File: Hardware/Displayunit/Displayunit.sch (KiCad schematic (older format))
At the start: 111 parts, among them IC1 TSC2007, IC2 MX25LM51245GXDI00, IC3 IS66WVH8M8BLL-100B1LI_0, J1 USB_B_Micro, J2 8P8C_Shielded, J3 54104-4031, J4 Conn_ARM_JTAG_SWD_20, J5 52271-0679, J6 Conn_02x06_Odd_Even, J7 734-264, Q1 2N7002, SW1 Boot, SW2 Reset, SW3 Wakeup, U1 STM32L4R9ZITx, U2 USBLC6-2SC6, U3 STLD40D, U4 MAX17572, U5 MAX17572, U6 SN65HVD231, Y1 16 MHz, Y2 32.768

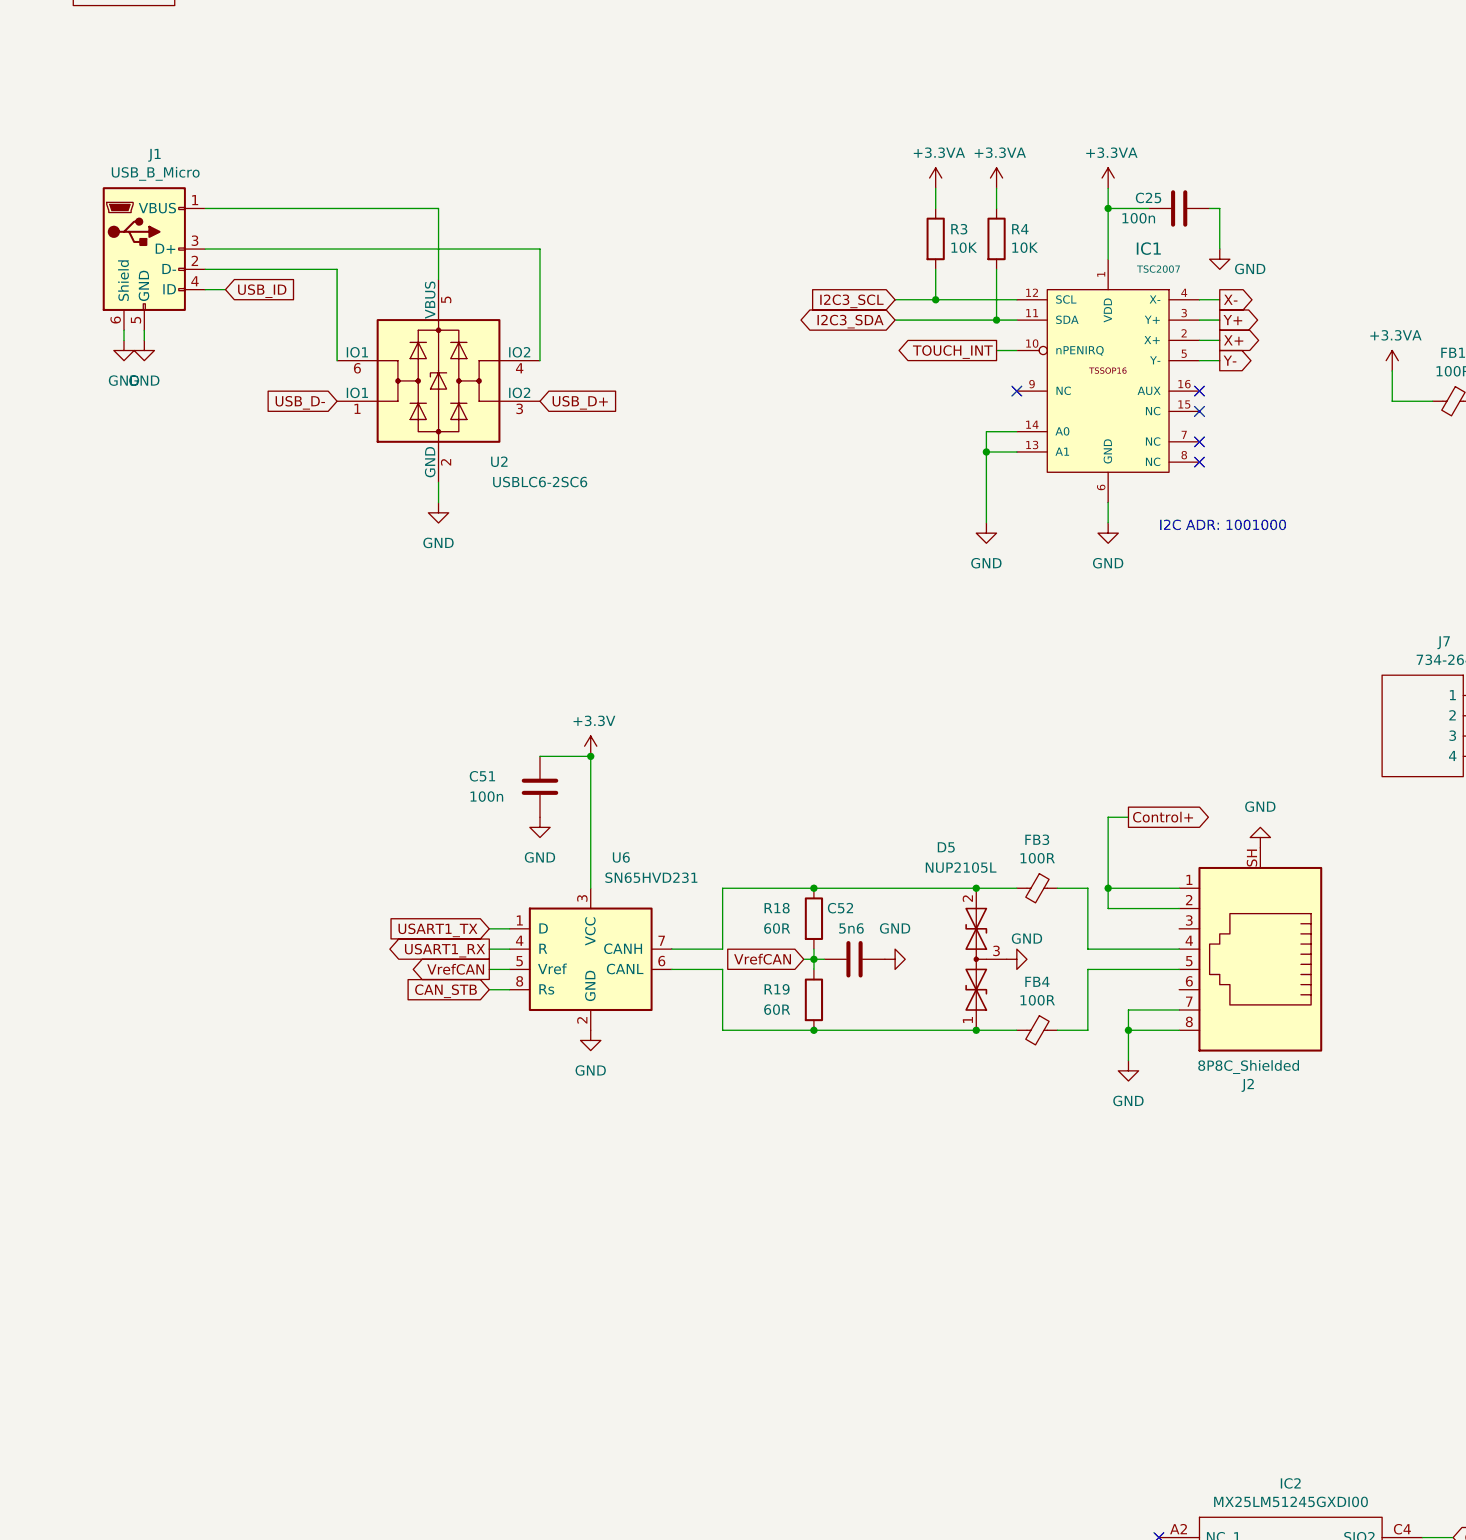
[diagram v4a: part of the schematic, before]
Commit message: Displayunit: Zweite Controlbus Buchse hinzugefügt.
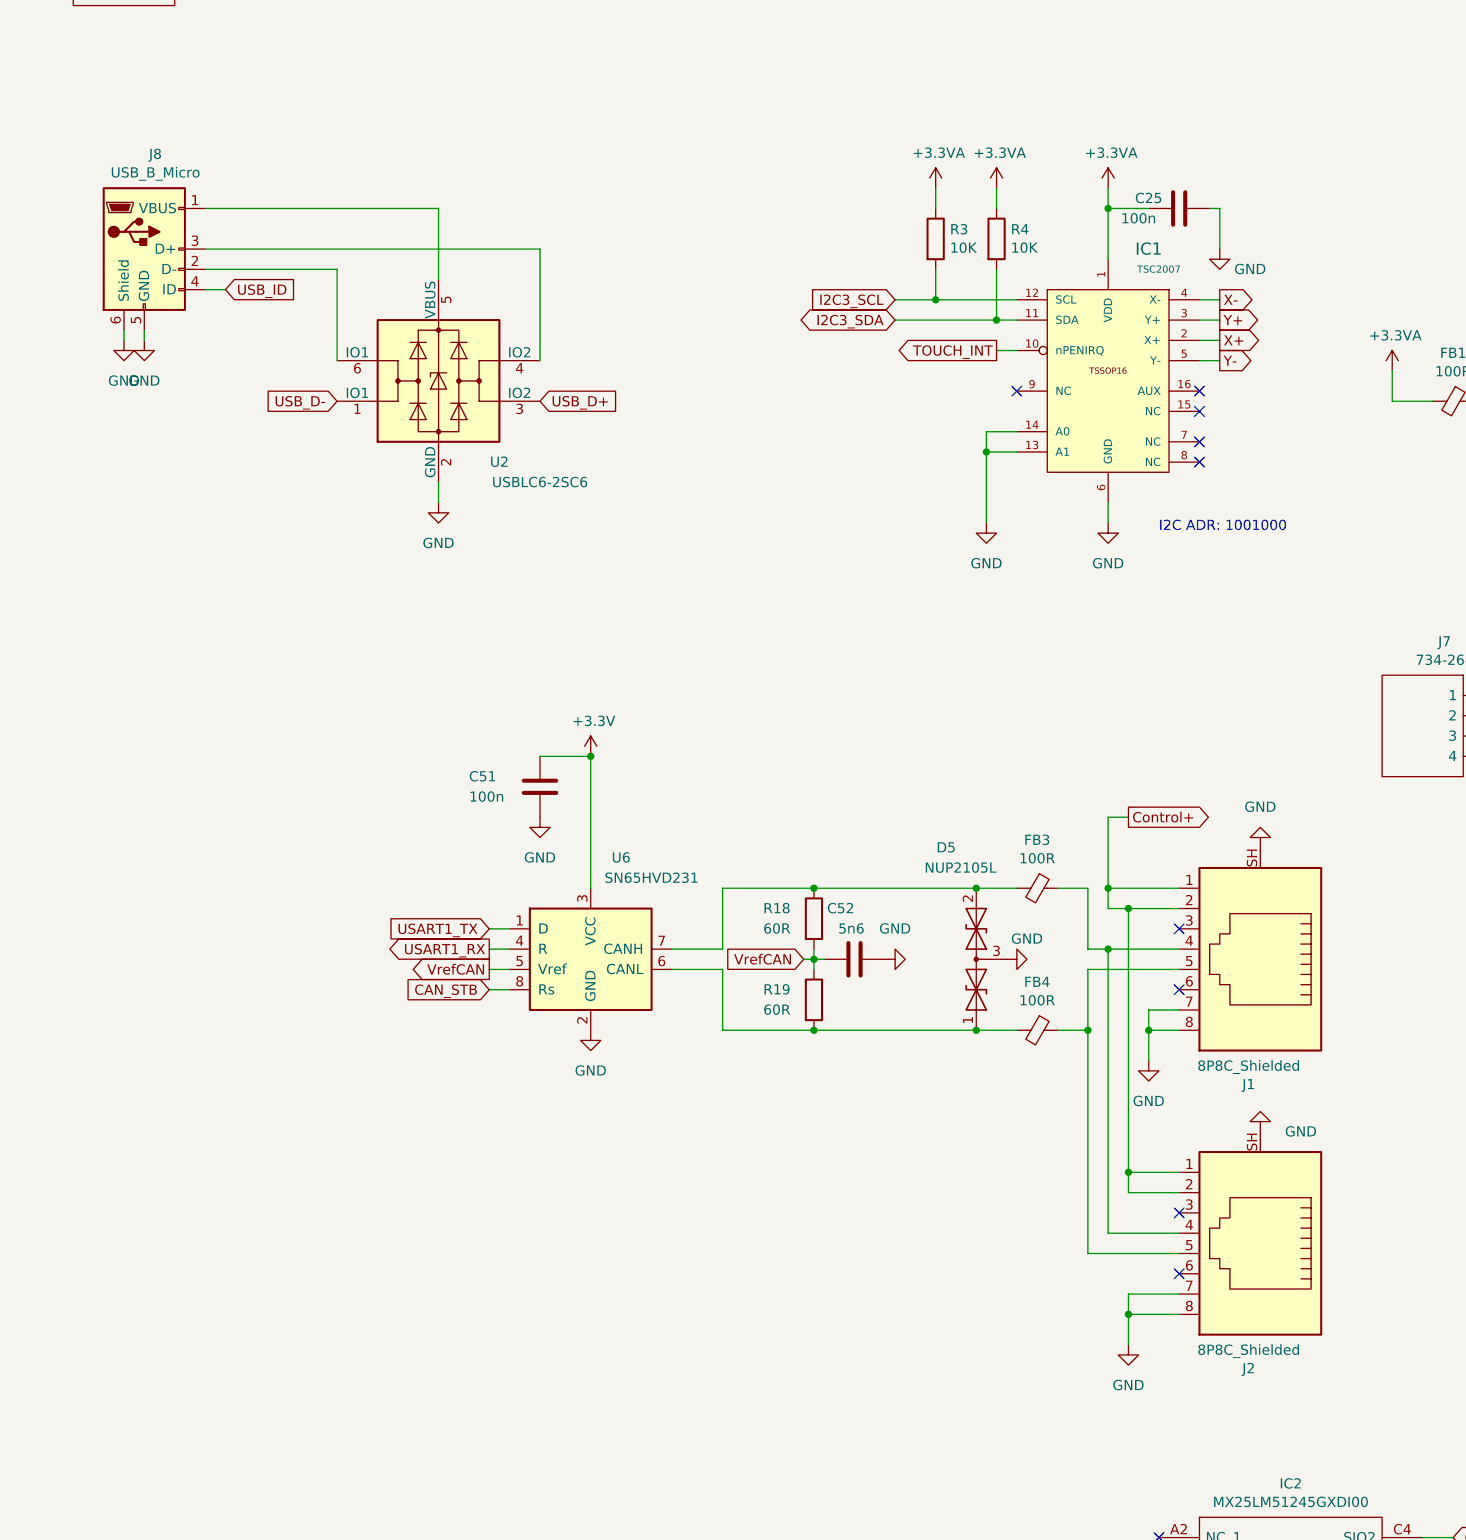
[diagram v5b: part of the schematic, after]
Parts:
- added J2: 8P8C_Shielded, Connector_RJ:RJ45_Amphenol_RJHSE5380, symbol Displayunit-rescue:8P8C_Shielded-Connector
- renumbered J2 to J1, J1 to J8
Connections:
- net Control+: now also J2.1, J2.2
- net GND: now also J2.7, J2.8, J2.SH
- net at FB3.1, J1.4: now also J2.4
- net at FB4.1, J1.5: now also J2.5
- no-connect marks 22 -> 26
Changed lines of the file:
@@
 EESchema Schematic File Version 4
 LIBS:Displayunit-cache
-EELAYER 30 0
+EELAYER 29 0
 EELAYER END
 $Descr A2 23386 16535
@@
 P 10400 5000
 AR Path="/5D80E2A0/5E312421" Ref="J?"  Part="1"
-AR Path="/5E312421" Ref="J1"  Part="1"
-F 0 "J1" H 10455 5467 50  0000 C CNN
+AR Path="/5E312421" Ref="J8"  Part="1"
+F 0 "J8" H 10455 5467 50  0000 C CNN
 F 1 "USB_B_Micro" H 10455 5376 50  0000 C CNN
 F 2 "Connector_USB:USB_Micro-B_Molex-105017-0001" H 10550 4950 50  0001 C CNN
@@
 Y-
 $Comp
-L Displayunit-rescue:8P8C_Shielded-Connector J2
+L Displayunit-rescue:8P8C_Shielded-Connector J1
 U 1 1 5F96FCE3
 P 15900 8450
-F 0 "J2" H 15957 9117 50  0000 C CNN
+F 0 "J1" H 15957 9117 50  0000 C CNN
 F 1 "8P8C_Shielded" H 15957 9026 50  0000 C CNN
 F 2 "Connector_RJ:RJ45_Amphenol_RJHSE5380" V 15900 8475 50  0001 C CNN
@@
 	15050 8150 15050 8450
 Wire Wire Line
-	15050 8450 15500 8450
+	15050 8450 15150 8450
 Wire Wire Line
 	15500 8550 15050 8550
@@
 Control+
 Wire Wire Line
-	15500 8250 15150 8250
+	15500 8250 15250 8250
 Wire Wire Line
 	15150 8250 15150 8150
@@
 L Displayunit-rescue:GND-power #PWR?
 U 1 1 5ECB14B9
-P 15250 9000
+P 15350 9000
 AR Path="/5C8BBC9A/5ECB14B9" Ref="#PWR?"  Part="1"
 AR Path="/5E0C5EEA/5ECB14B9" Ref="#PWR?"  Part="1"
@@
 AR Path="/5D80E2A0/5ECB14B9" Ref="#PWR?"  Part="1"
 AR Path="/5ECB14B9" Ref="#PWR0114"  Part="1"
-F 0 "#PWR0114" H 15250 8750 50  0001 C CNN
-F 1 "GND" H 15250 8800 50  0000 C CNN
-F 2 "" H 15250 9000 50  0001 C CNN
-F 3 "" H 15250 9000 50  0001 C CNN
-	1    15250 9000
+F 0 "#PWR0114" H 15350 8750 50  0001 C CNN
+F 1 "GND" H 15350 8800 50  0000 C CNN
+F 2 "" H 15350 9000 50  0001 C CNN
+F 3 "" H 15350 9000 50  0001 C CNN
+	1    15350 9000
 	1    0    0    -1
 $EndComp
-Wire Wire Line
-	15500 8750 15250 8750
-Wire Wire Line
-	15250 8750 15250 8850
-Wire Wire Line
-	15500 8850 15250 8850
-Connection ~ 15250 8850
-Wire Wire Line
-	15250 8850 15250 9000
 $Comp
 L Displayunit-rescue:+3.3VA-power #PWR?
@@
 Wire Wire Line
 	17500 4150 17400 4150
+$Comp
+L Displayunit-rescue:8P8C_Shielded-Connector J2
+U 1 1 5DED998B
+P 15900 9850
+F 0 "J2" H 15957 10517 50  0000 C CNN
+F 1 "8P8C_Shielded" H 15957 10426 50  0000 C CNN
+F 2 "Connector_RJ:RJ45_Amphenol_RJHSE5380" V 15900 9875 50  0001 C CNN
+F 3 "~" V 15900 9875 50  0001 C CNN
+	1    15900 9850
+	-1   0    0    1
+$EndComp
+$Comp
+L Displayunit-rescue:GND-power #PWR?
+U 1 1 5DEDCC16
+P 15250 10400
+AR Path="/5C8BBC9A/5DEDCC16" Ref="#PWR?"  Part="1"
+AR Path="/5E0C5EEA/5DEDCC16" Ref="#PWR?"  Part="1"
+AR Path="/5D80EC74/5DEDCC16" Ref="#PWR?"  Part="1"
+AR Path="/5D80E6E8/5DEDCC16" Ref="#PWR?"  Part="1"
+AR Path="/5D80E2A0/5DEDCC16" Ref="#PWR?"  Part="1"
+AR Path="/5DEDCC16" Ref="#PWR?"  Part="1"
+F 0 "#PWR?" H 15250 10150 50  0001 C CNN
+F 1 "GND" H 15250 10200 50  0000 C CNN
+F 2 "" H 15250 10400 50  0001 C CNN
+F 3 "" H 15250 10400 50  0001 C CNN
+	1    15250 10400
+	1    0    0    -1
+$EndComp
+Wire Wire Line
+	15500 10150 15250 10150
+Wire Wire Line
+	15250 10150 15250 10250
+Wire Wire Line
+	15500 10250 15250 10250
+Connection ~ 15250 10250
+Wire Wire Line
+	15250 10250 15250 10400
+Wire Wire Line
+	15500 9950 15050 9950
+Wire Wire Line
+	15050 9950 15050 8850
+Connection ~ 15050 8850
+Wire Wire Line
+	15500 9850 15150 9850
+Wire Wire Line
+	15150 9850 15150 8450
+Connection ~ 15150 8450
+Wire Wire Line
+	15150 8450 15500 8450
+Wire Wire Line
+	15350 8750 15350 8850
+Wire Wire Line
+	15500 8750 15350 8750
+Wire Wire Line
+	15500 8850 15350 8850
+Connection ~ 15350 8850
+Wire Wire Line
+	15350 8850 15350 9000
+Wire Wire Line
+	15500 9650 15250 9650
+Wire Wire Line
+	15250 9650 15250 9550
+Connection ~ 15250 8250
+Wire Wire Line
+	15250 8250 15150 8250
+Wire Wire Line
+	15500 9550 15250 9550
+Connection ~ 15250 9550
+Wire Wire Line
+	15250 9550 15250 8250
+NoConn ~ 15500 8350
+NoConn ~ 15500 8650
+NoConn ~ 15500 9750
+NoConn ~ 15500 10050
+$Comp
+L Displayunit-rescue:GND-power #PWR?
+U 1 1 5E47C766
+P 15900 9350
+AR Path="/5C8BBC9A/5E47C766" Ref="#PWR?"  Part="1"
+AR Path="/5E0C5EEA/5E47C766" Ref="#PWR?"  Part="1"
+AR Path="/5D80EC74/5E47C766" Ref="#PWR?"  Part="1"
+AR Path="/5D80E6E8/5E47C766" Ref="#PWR?"  Part="1"
+AR Path="/5D80E2A0/5E47C766" Ref="#PWR?"  Part="1"
+AR Path="/5E47C766" Ref="#PWR?"  Part="1"
+F 0 "#PWR?" H 15900 9100 50  0001 C CNN
+F 1 "GND" H 15700 9350 50  0000 C CNN
+F 2 "" H 15900 9350 50  0001 C CNN
+F 3 "" H 15900 9350 50  0001 C CNN
+	1    15900 9350
+	-1   0    0    1
+$EndComp
 $EndSCHEMATC

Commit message: Displayboard: Flex Stecker Position festgelegt, verschiebung von Componenten.
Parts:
- removed J7: 734-264, WAGO:SHDR4W120P0X381_1X4_1640X1030X850P, symbol WAGO:734-264
- removed R2: 10K, Resistor_SMD:R_0603_1608Metric, symbol Displayunit-rescue:R-Device
- removed SW3: Wakeup, Button_Switch_THT:SW_PUSH_6mm_H8.5mm, symbol Displayunit-rescue:SW_Push-Switch
- added J7: WAGO_Klemmleiste_2-pol, WAGO:WAGO_Klemmleiste_Hebel4mm²Horizontal_RM5mm_2-pol, symbol WAGO:WAGO_Klemmleiste_2-pol
- added J9: Conn_02x05_Odd_Even, Connector_IDC:IDC-Header_2x05_P2.54mm_Vertical, symbol Connector_Generic:Conn_02x05_Odd_Even
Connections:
- net GND: now also J7.2 (Pin_2)
- net at C53.1, D2.2 (A): now also J7.1 (Pin_1)
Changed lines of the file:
@@
 EESchema Schematic File Version 4
 LIBS:Displayunit-cache
-EELAYER 29 0
+EELAYER 30 0
 EELAYER END
 $Descr A2 23386 16535
@@
 $Comp
 L Displayunit-rescue:+3.3V-power #PWR?
-U 1 1 5E31291D
-P 3900 4050
-AR Path="/5D80E2A0/5E31291D" Ref="#PWR?"  Part="1"
-AR Path="/5E31291D" Ref="#PWR010"  Part="1"
-F 0 "#PWR010" H 3900 3900 50  0001 C CNN
-F 1 "+3.3V" H 3915 4223 50  0000 C CNN
-F 2 "" H 3900 4050 50  0001 C CNN
-F 3 "" H 3900 4050 50  0001 C CNN
-	1    3900 4050
-	1    0    0    -1
-$EndComp
-$Comp
-L Displayunit-rescue:+3.3V-power #PWR?
 U 1 1 5E312917
 P 2950 4050
@@
 $Comp
 L Displayunit-rescue:GND-power #PWR?
-U 1 1 5E312845
-P 3900 5050
-AR Path="/5C8BBC9A/5E312845" Ref="#PWR?"  Part="1"
-AR Path="/5E0C5EEA/5E312845" Ref="#PWR?"  Part="1"
-AR Path="/5D80EC74/5E312845" Ref="#PWR?"  Part="1"
-AR Path="/5D80E6E8/5E312845" Ref="#PWR?"  Part="1"
-AR Path="/5D80E2A0/5E312845" Ref="#PWR?"  Part="1"
-AR Path="/5E312845" Ref="#PWR011"  Part="1"
-F 0 "#PWR011" H 3900 4800 50  0001 C CNN
-F 1 "GND" H 3900 4850 50  0000 C CNN
-F 2 "" H 3900 5050 50  0001 C CNN
-F 3 "" H 3900 5050 50  0001 C CNN
-	1    3900 5050
-	1    0    0    -1
-$EndComp
-$Comp
-L Displayunit-rescue:GND-power #PWR?
 U 1 1 5E31283F
 P 2950 5050
@@
 Signal_LED
 Wire Wire Line
-	3900 5050 3900 4950
-Connection ~ 3900 4500
-Wire Wire Line
-	3900 4550 3900 4500
-Wire Wire Line
-	3900 4500 3900 4450
-Wire Wire Line
-	4000 4500 3900 4500
-Text GLabel 4000 4500 2    50   Output ~ 0
-Wakeup
-$Comp
-L Displayunit-rescue:R-Device R?
-U 1 1 5E31278B
-P 3900 4300
-AR Path="/5D80E2A0/5E31278B" Ref="R?"  Part="1"
-AR Path="/5E31278B" Ref="R2"  Part="1"
-F 0 "R2" H 3970 4346 50  0000 L CNN
-F 1 "10K" H 3970 4255 50  0000 L CNN
-F 2 "Resistor_SMD:R_0603_1608Metric" V 3830 4300 50  0001 C CNN
-F 3 "~" H 3900 4300 50  0001 C CNN
-	1    3900 4300
-	1    0    0    -1
-$EndComp
-Wire Wire Line
-	3900 4050 3900 4150
-$Comp
-L Displayunit-rescue:SW_Push-Switch SW?
-U 1 1 5E312784
-P 3900 4750
-AR Path="/5D80E2A0/5E312784" Ref="SW?"  Part="1"
-AR Path="/5E312784" Ref="SW3"  Part="1"
-F 0 "SW3" V 3900 5035 50  0000 C CNN
-F 1 "Wakeup" V 3800 5000 50  0000 C CNN
-F 2 "Button_Switch_THT:SW_PUSH_6mm_H8.5mm" H 3900 4950 50  0001 C CNN
-F 3 "" H 3900 4950 50  0001 C CNN
-	1    3900 4750
-	0    -1   -1   0
-$EndComp
-Wire Wire Line
 	7400 8300 7250 8300
 Text GLabel 7400 8300 2    50   Input ~ 0
@@
 	1    0    0    -1
 $EndComp
-$Comp
-L WAGO:734-264 J7
-U 1 1 5E4409BD
-P 17100 7200
-F 0 "J7" H 17392 7465 50  0000 C CNN
-F 1 "734-264" H 17392 7374 50  0000 C CNN
-F 2 "WAGO:SHDR4W120P0X381_1X4_1640X1030X850P" H 17750 7300 50  0001 L CNN
-F 3 "https://www.wago.com/global/pluggable-connectors/tht-male-header/p/734-264" H 17750 7200 50  0001 L CNN
-F 4 "WAGO - 734-264 - Terminal Block, Header, 3.81 mm, 4 Ways, 10 A, 300 V, Through Hole Right Angle" H 17750 7100 50  0001 L CNN "Description"
-F 5 "8.5" H 17750 7000 50  0001 L CNN "Height"
-F 6 "Wago" H 17750 6900 50  0001 L CNN "Manufacturer_Name"
-F 7 "734-264" H 17750 6800 50  0001 L CNN "Manufacturer_Part_Number"
-F 8 "" H 17750 6700 50  0001 L CNN "Mouser Part Number"
-F 9 "" H 17750 6600 50  0001 L CNN "Mouser Price/Stock"
-F 10 "" H 17750 6500 50  0001 L CNN "RS Part Number"
-F 11 "" H 17750 6400 50  0001 L CNN "RS Price/Stock"
-	1    17100 7200
-	-1   0    0    -1
-$EndComp
 Wire Wire Line
 	19300 7200 19550 7200
@@
 $EndComp
 Wire Wire Line
-	17100 7400 17200 7400
-Wire Wire Line
-	17200 7400 17200 7500
-Wire Wire Line
-	17100 7500 17200 7500
-Connection ~ 17200 7500
-Wire Wire Line
-	17200 7500 17200 7650
-Wire Wire Line
-	17100 7300 17400 7300
-Wire Wire Line
-	17400 7300 17400 7350
-Wire Wire Line
 	17100 7200 17400 7200
-Wire Wire Line
-	17400 7200 17400 7300
-Connection ~ 17400 7300
 Connection ~ 17400 7200
 Wire Wire Line
@@
 AR Path="/5D80E6E8/5DEDCC16" Ref="#PWR?"  Part="1"
 AR Path="/5D80E2A0/5DEDCC16" Ref="#PWR?"  Part="1"
-AR Path="/5DEDCC16" Ref="#PWR?"  Part="1"
-F 0 "#PWR?" H 15250 10150 50  0001 C CNN
+AR Path="/5DEDCC16" Ref="#PWR0122"  Part="1"
+F 0 "#PWR0122" H 15250 10150 50  0001 C CNN
 F 1 "GND" H 15250 10200 50  0000 C CNN
 F 2 "" H 15250 10400 50  0001 C CNN
@@
 AR Path="/5D80E6E8/5E47C766" Ref="#PWR?"  Part="1"
 AR Path="/5D80E2A0/5E47C766" Ref="#PWR?"  Part="1"
-AR Path="/5E47C766" Ref="#PWR?"  Part="1"
-F 0 "#PWR?" H 15900 9100 50  0001 C CNN
+AR Path="/5E47C766" Ref="#PWR0123"  Part="1"
+F 0 "#PWR0123" H 15900 9100 50  0001 C CNN
 F 1 "GND" H 15700 9350 50  0000 C CNN
 F 2 "" H 15900 9350 50  0001 C CNN
@@
 	-1   0    0    1
 $EndComp
+$Comp
+L WAGO:WAGO_Klemmleiste_2-pol J7
+U 1 1 5DF16CB3
+P 16900 7200
+F 0 "J7" H 16818 7417 50  0000 C CNN
+F 1 "WAGO_Klemmleiste_2-pol" H 16818 7326 50  0000 C CNN
+F 2 "WAGO:WAGO_Klemmleiste_Hebel4mm²Horizontal_RM5mm_2-pol" H 16900 7200 50  0001 C CNN
+F 3 "~" H 16900 7200 50  0001 C CNN
+	1    16900 7200
+	-1   0    0    -1
+$EndComp
+Wire Wire Line
+	17400 7200 17400 7350
+Wire Wire Line
+	17100 7300 17200 7300
+Wire Wire Line
+	17200 7300 17200 7650
+$Comp
+L Connector_Generic:Conn_02x05_Odd_Even J9
+U 1 1 5E0F2A56
+P 13050 2400
+F 0 "J9" H 13100 2817 50  0000 C CNN
+F 1 "Conn_02x05_Odd_Even" H 13100 2726 50  0000 C CNN
+F 2 "Connector_IDC:IDC-Header_2x05_P2.54mm_Vertical" H 13050 2400 50  0001 C CNN
+F 3 "~" H 13050 2400 50  0001 C CNN
+	1    13050 2400
+	1    0    0    -1
+$EndComp
 $EndSCHEMATC

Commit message: Displayboard: Layout
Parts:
- added C55: 1uF, Capacitor_SMD:C_1210_3225Metric, symbol Displayunit-rescue:C-Device
- added C56: 100n, Capacitor_SMD:C_0603_1608Metric, symbol Displayunit-rescue:C-Device
- added FB10, FB5, FB6, FB7, FB8, FB9: 100R, Inductor_SMD:L_0603_1608Metric, symbol Displayunit-rescue:Ferrite_Bead_Small-Device
- added U7: AT25xxx, Package_SO:SO-8_3.9x4.9mm_P1.27mm, symbol Memory_EEPROM:AT25xxx
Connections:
- net *LCD_LED-A is gone; now on net LCD_LED-A: J3.2
- net *LCD_LED-K is gone; now on net LCD_LED-K: J3.1
- net LCD_INT is gone; now on net TOUCH_RESET: U1.101 (PC9)
- net +3V3: now also C56.1, FB10.1, U7.3 (~WP), U7.7 (~HOLD), U7.8 (VCC)
- net GND: now also J9.10 (Pin_10), J9.6 (Pin_6), J9.8 (Pin_8), C55.2, C56.2, U7.4 (GND)
- net I2C3_SCL: now also FB8.2; no longer IC1.12 (SCL), J5.3, J6.1 (Pin_1), R3.2
- net I2C3_SDA: now also FB9.2; no longer IC1.11 (SDA), J5.4, J6.3 (Pin_3), R4.2
- net SPI1_MISO: now also U7.2 (MISO)
- net SPI1_MOSI: now also U7.5 (MOSI)
- net SPI1_NSS: now also U7.1 (~CS)
- net SPI1_SCK: now also U7.6 (SCK)
- net USART1_RX: now also U1.137 (PB7)
- net USART1_TX: now also U1.136 (PB6)
- net at J9.1 (Pin_1): now also FB5.1
- net at J9.2 (Pin_2): now also J9.4 (Pin_4), C55.1, FB10.2
- net at J9.3 (Pin_3): now also FB6.1
- net at J9.5 (Pin_5): now also FB7.1
- net at J9.7 (Pin_7): now also FB8.1
- net at J9.9 (Pin_9): now also FB9.1
- net EXT_1: now reaches U1.139 (PB8)
- net EXT_1: now also FB5.2
- net EXT_2: now reaches U1.140 (PB9)
- net EXT_2: now also FB6.2
- net EXT_3: now reaches U1.65 (PB10)
- net EXT_3: now also FB7.2
- net *I2C2_SCL renamed I2C2_SCL
- net I2C2_SCL: now also IC1.12 (SCL), J5.3, J6.1 (Pin_1), R3.2
- net *I2C2_SDA renamed I2C2_SDA
- net I2C2_SDA: now also IC1.11 (SDA), J5.4, J6.3 (Pin_3), R4.2
- net *I2C4_SCL renamed I2C4_SCL
- net *I2C4_SDA renamed I2C4_SDA
- net *LCD_BL_CTR renamed LCD_BL_CTR
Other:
- moved on the sheet: C26, J3, J9
